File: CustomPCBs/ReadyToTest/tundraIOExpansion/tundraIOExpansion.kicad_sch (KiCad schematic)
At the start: 58 parts, among them J1 Conn_01x25, J2 Conn_ARM_SWD_TagConnect_TC203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, J3 Conn_ARM_SWD_TagConnect_TC203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, U1 RP2040, U2 MX25L3233FM2, U4 MX25L3233FM2, U5 RP2040, Y1 12.000MHz, Y2 12.000MHz, Y3 32.768kHz

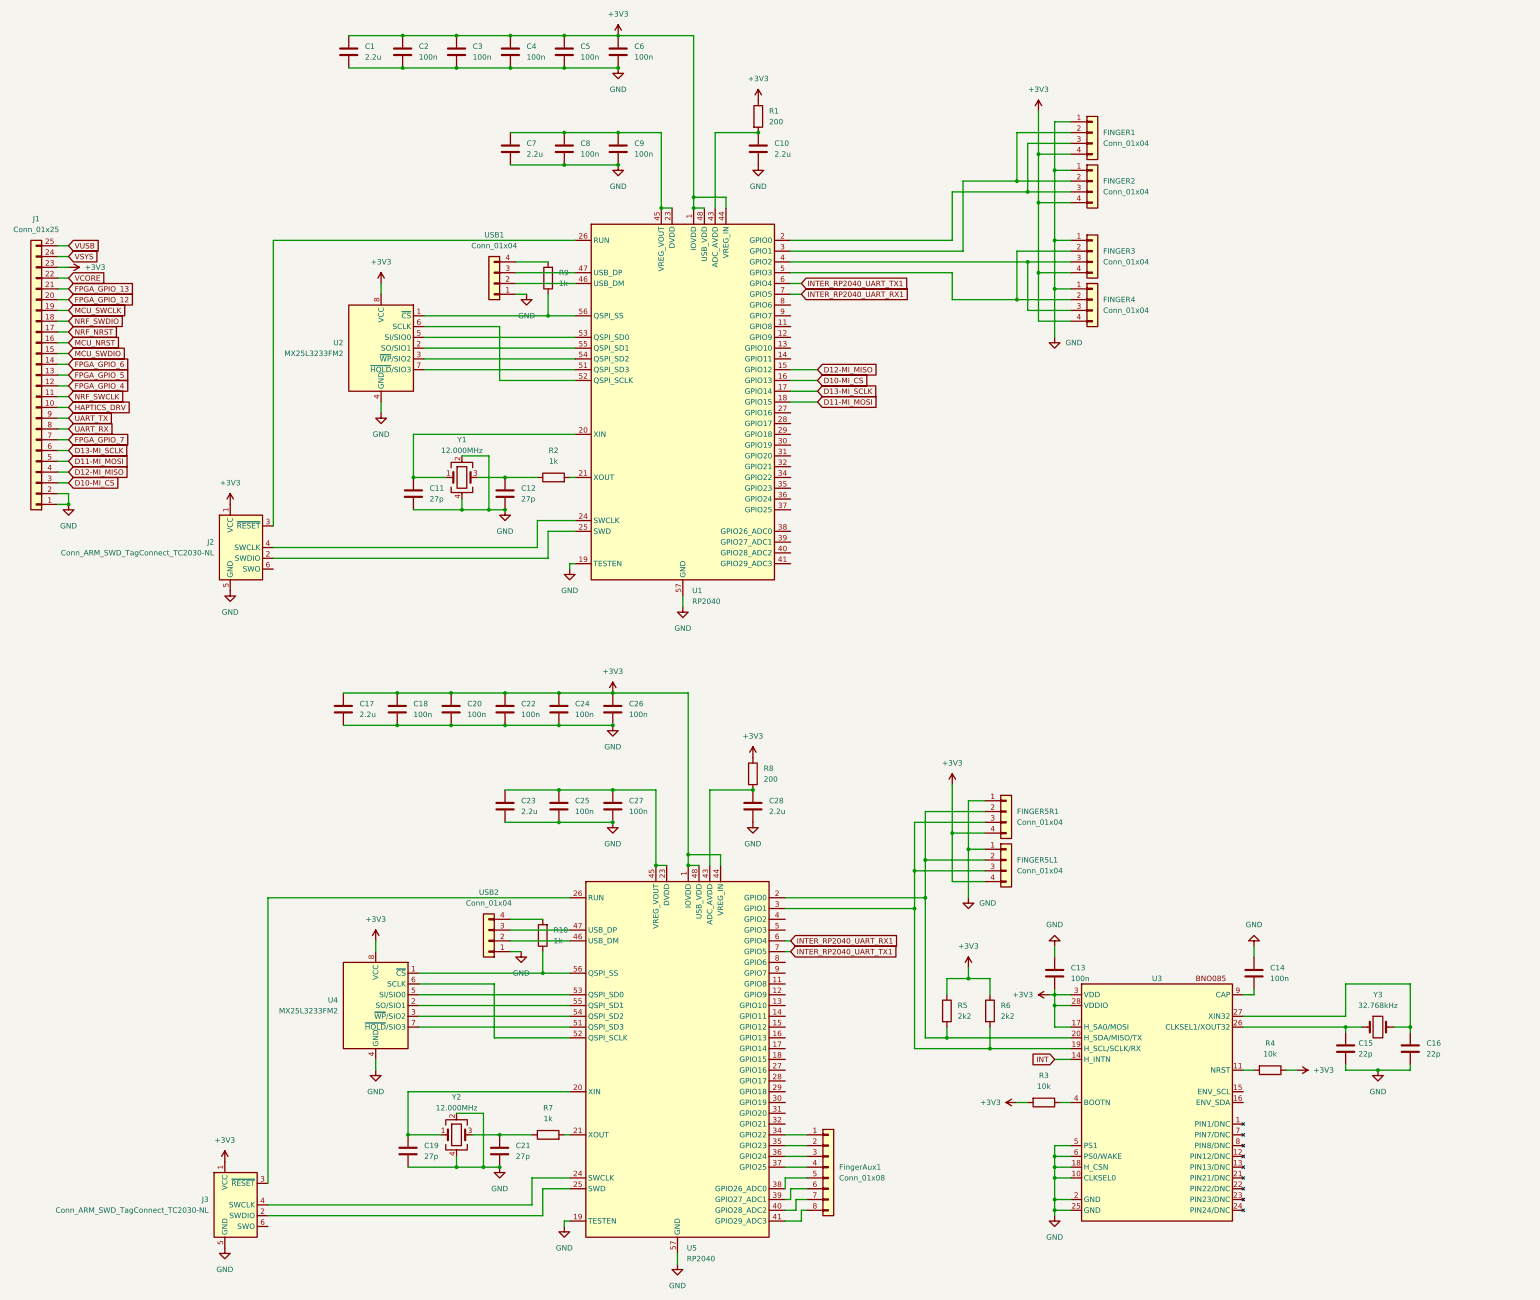
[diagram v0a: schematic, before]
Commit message: Fixing mistakes on the main board
Flash chip was not the recommended by raspberry pi foundation - fixed.
SCL and SDA pins on the thumb JST connectors were switched - fixed.
MOSI and MISO pins on the RP2040 were switched - fixed.
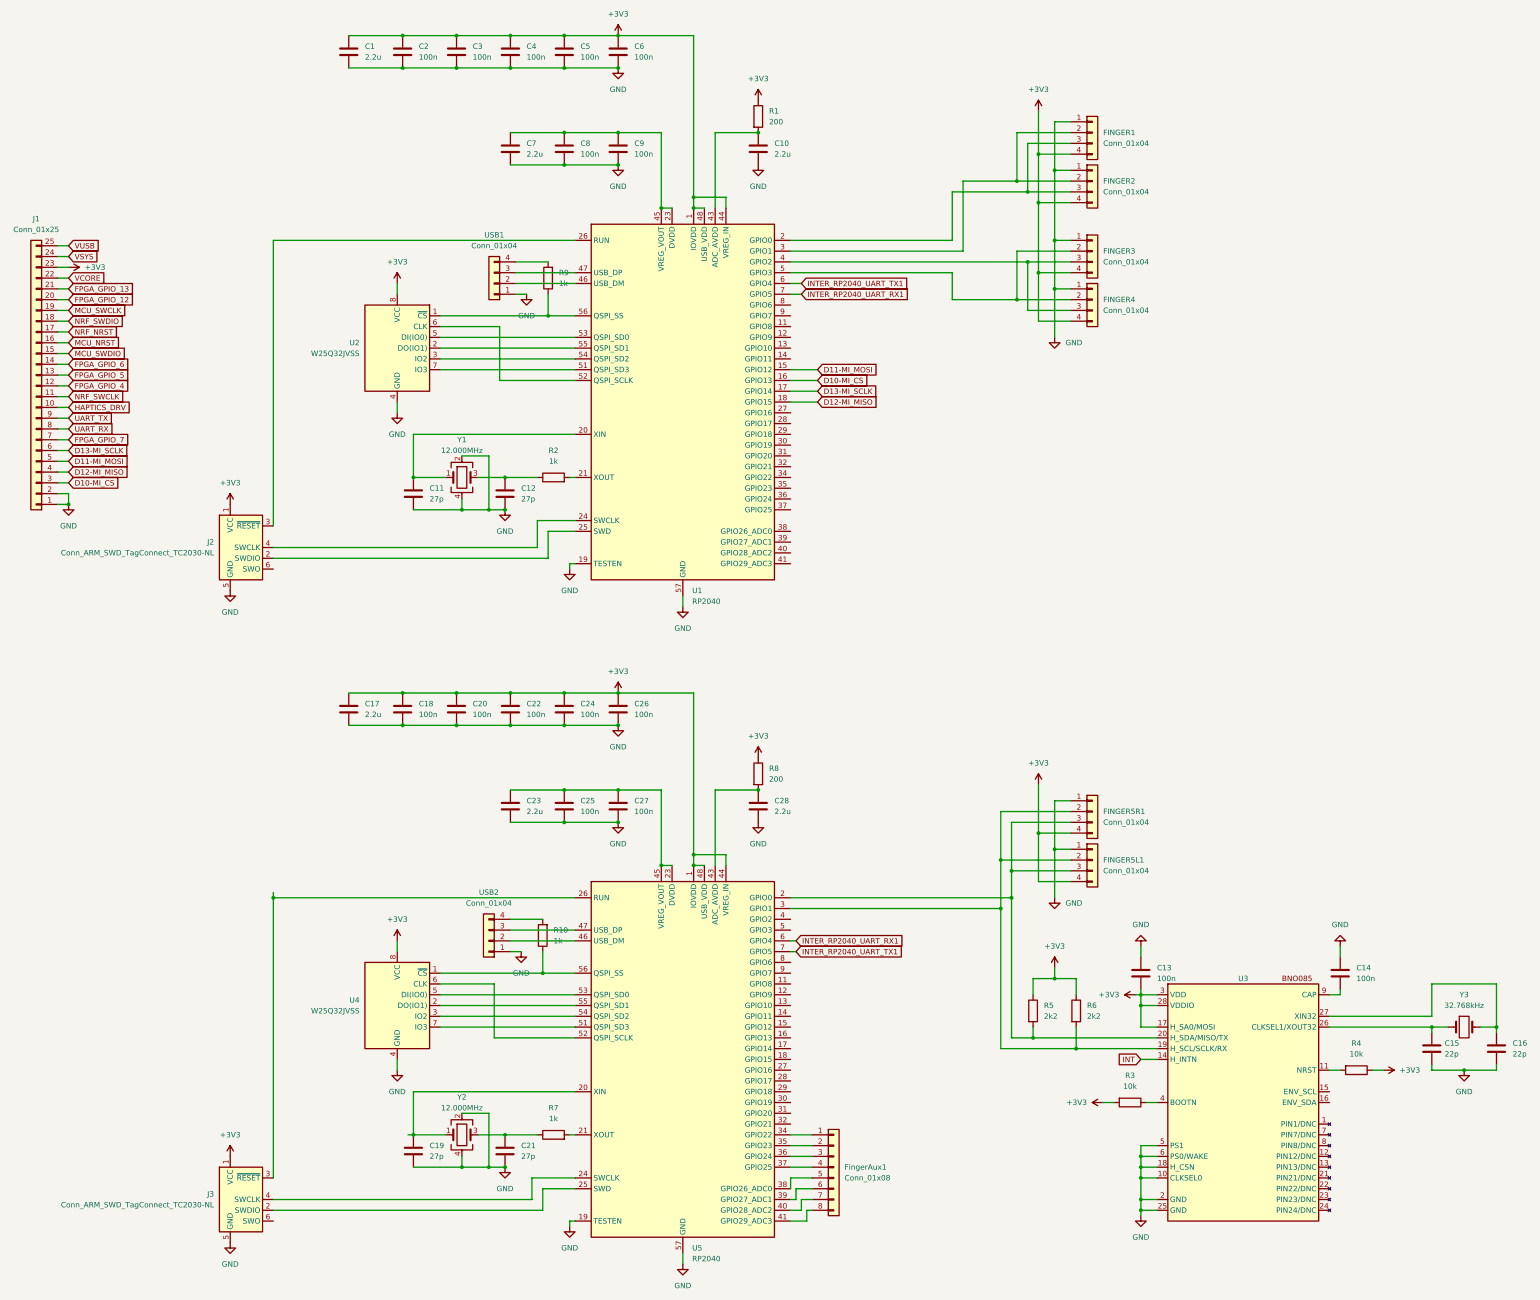
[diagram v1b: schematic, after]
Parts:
- removed U2, U4: MX25L3233FM2, Package_SO:SOP-8_5.28x5.23mm_P1.27mm, symbol Memory_Flash:MX25L3233FM2
- added U2, U4: W25Q32JVSS, Package_SO:SOIC-8_5.23x5.23mm_P1.27mm, symbol Memory_Flash:W25Q32JVSS
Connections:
- net +3V3: now also U2.8 (VCC), U4.8 (VCC)
- net D11-MI_MOSI: now also U1.15 (GPIO12); no longer U1.18 (GPIO15)
- net D12-MI_MISO: now also U1.18 (GPIO15); no longer U1.15 (GPIO12)
- net GND: now also U2.4 (GND), U4.4 (GND)
- net at R5.2, U3.20 (H_SDA/MISO/TX), U5.2 (GPIO0): now also FINGER5L1.3 (Pin_3), FINGER5R1.3 (Pin_3); no longer FINGER5L1.2 (Pin_2), FINGER5R1.2 (Pin_2)
- net at U1.51 (QSPI_SD3): now also U2.7 (IO3)
- net at U1.52 (QSPI_SCLK): now also U2.6 (CLK)
- net at U1.53 (QSPI_SD0): now also U2.5 (DI(IO0))
- net at U1.54 (QSPI_SD2): now also U2.3 (IO2)
- net at U1.55 (QSPI_SD1): now also U2.2 (DO(IO1))
- net at R9.1, U1.56 (QSPI_SS): now also U2.1 (~{CS})
- net at R6.2, U3.19 (H_SCL/SCLK/RX), U5.3 (GPIO1): now also FINGER5L1.2 (Pin_2), FINGER5R1.2 (Pin_2); no longer FINGER5L1.3 (Pin_3), FINGER5R1.3 (Pin_3)
- net at R10.1, U5.56 (QSPI_SS): now also U4.1 (~{CS})
- net at U5.55 (QSPI_SD1): now also U4.2 (DO(IO1))
- net at U5.54 (QSPI_SD2): now also U4.3 (IO2)
- net at U5.53 (QSPI_SD0): now also U4.5 (DI(IO0))
- net at U5.52 (QSPI_SCLK): now also U4.6 (CLK)
- net at U5.51 (QSPI_SD3): now also U4.7 (IO3)
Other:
- moved on the sheet: C13, C14, C15, C16, C17, C18, C19, C20, C21, C22, C23, C24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
